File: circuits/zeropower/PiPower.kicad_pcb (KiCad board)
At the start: 2 copper layers, 65 x 30 mm, 6 parts, among them J1 GPIO, J2 171826-4

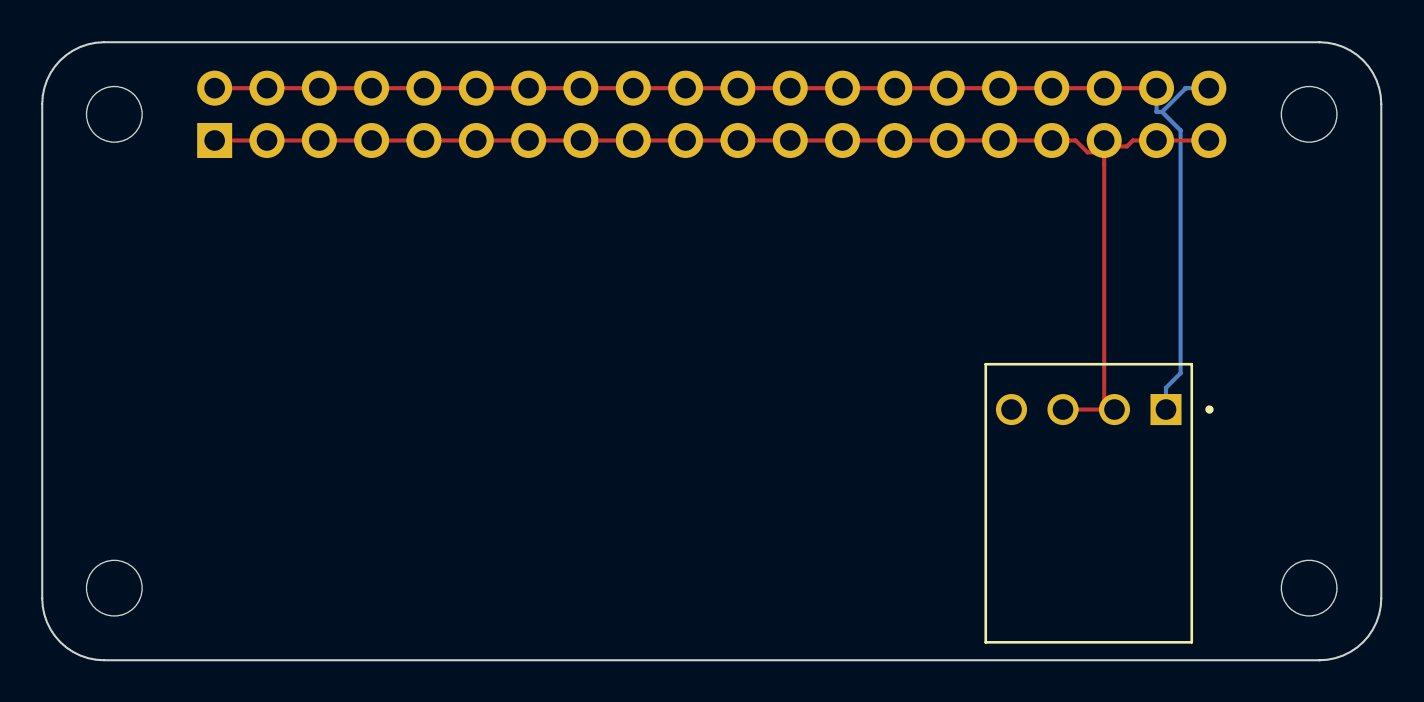
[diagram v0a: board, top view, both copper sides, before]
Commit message: Add silkscreen boardname and voltages
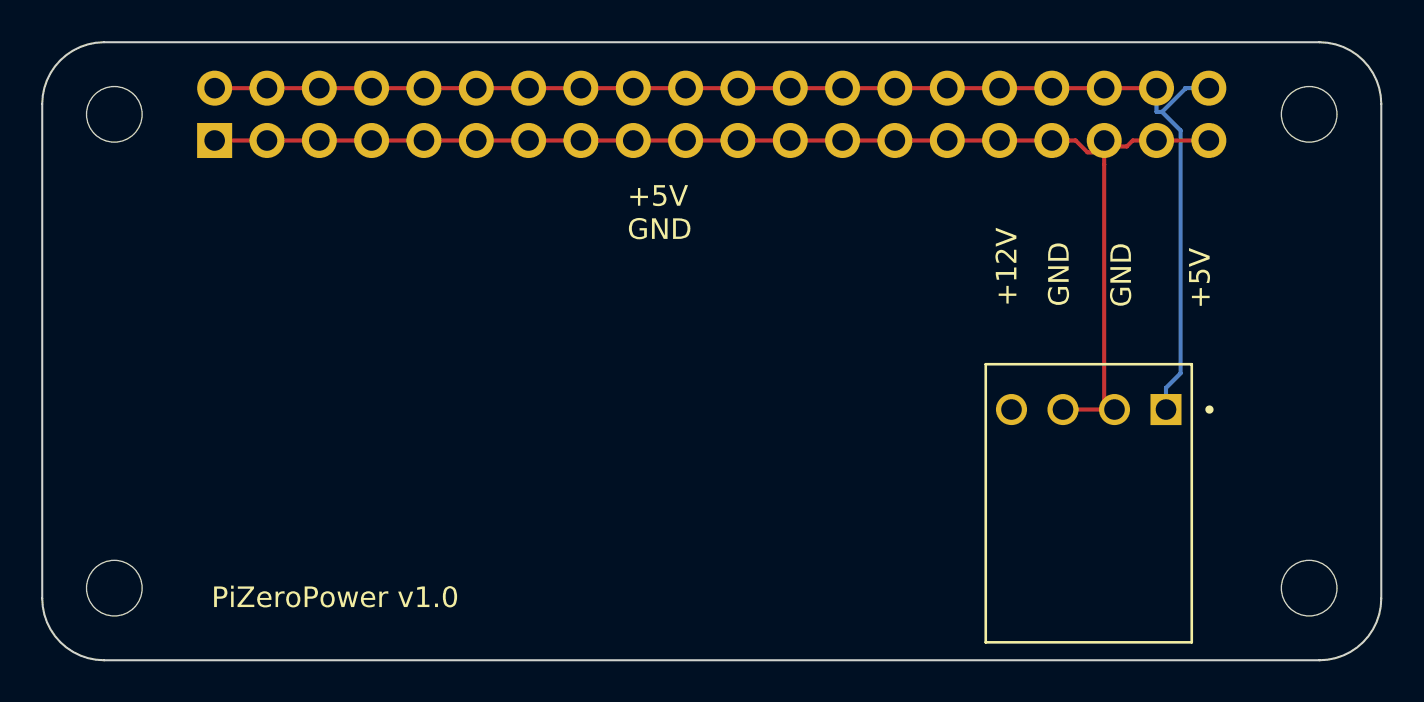
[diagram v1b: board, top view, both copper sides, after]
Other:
- board text added: "+12V"
- board text added: "+5V"
- board text added: "+5V GND"
- board text added: "GND"
- board text added: "PiZeroPower v1.0"
